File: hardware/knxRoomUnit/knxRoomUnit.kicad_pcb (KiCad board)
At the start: 2 copper layers, 65 x 42 mm, 69 parts, among them J1 PROG, J2 KNX, P1 ePaper FL, P2 ePaper, Q1 S8050, Q2 S8050, Q3 SI1308, SW1 RESET, SW2 KNX, SW3 DW, SW4 OK, SW5 UP, U1 ESP32-WROOM-32, U2 SHT31-DIS, U3 VCNL4040M3OE

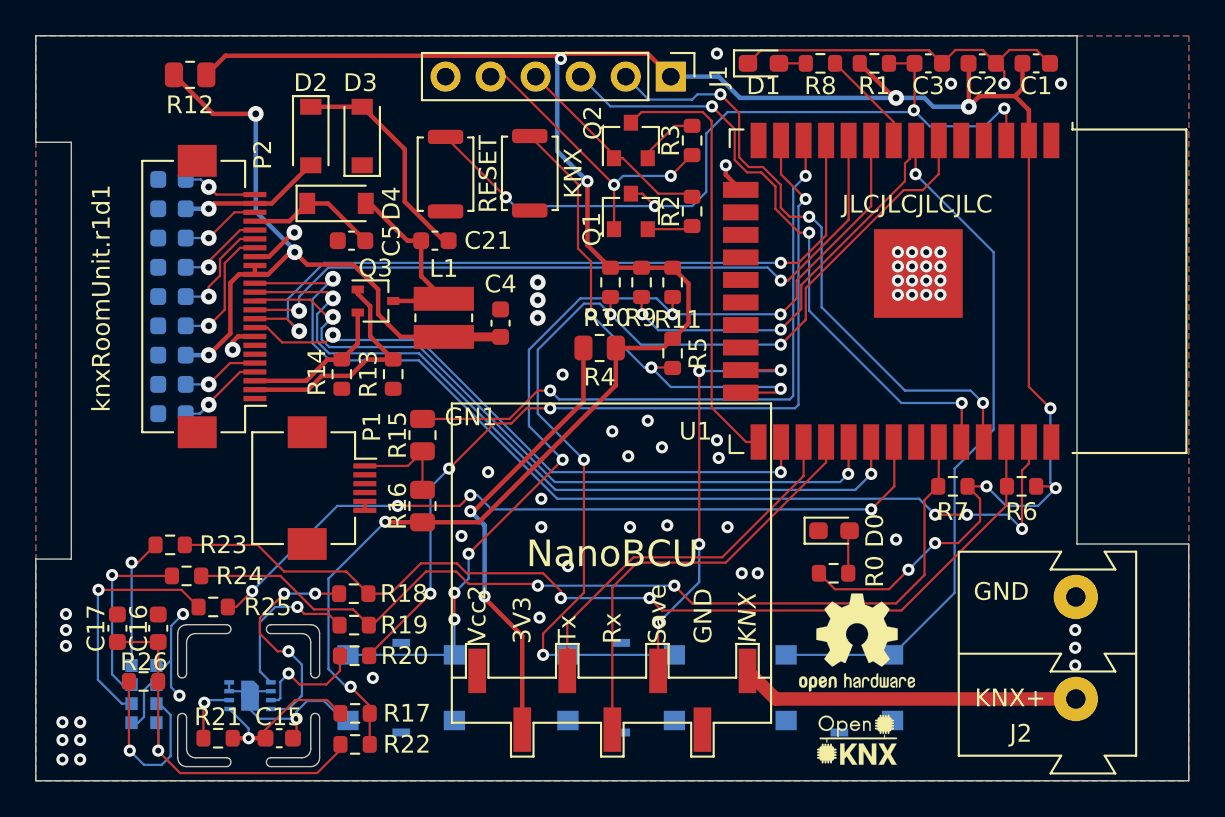
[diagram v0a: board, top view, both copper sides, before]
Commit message: Updated HW design
Changed R0/R8 to 470R
PCB routing and DRC
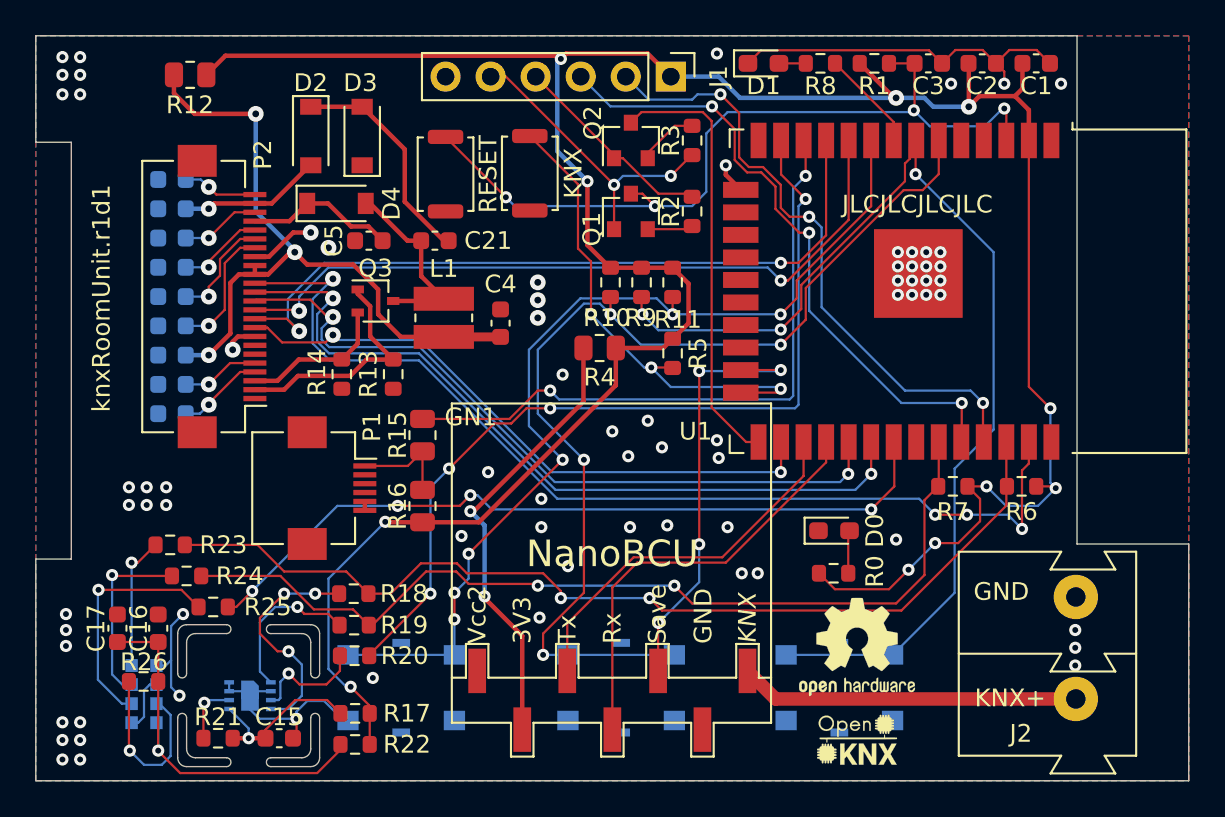
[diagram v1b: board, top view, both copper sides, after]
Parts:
- R0, R8: value 75 -> 470
- moved C5 0.98 mm to (106.8, 48.4)
- moved REF** 0.25 mm to (134.3, 71.2)
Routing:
- net /ePaper/PREVGH: track 7.51 -> 8.48 mm
- net GND: track 45.4 -> 46.4 mm, vias 61 -> 74
- net +3.3VA: track 39.4 -> 40.0 mm
